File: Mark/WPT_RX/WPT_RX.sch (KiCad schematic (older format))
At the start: 58 parts, among them J1 Conn_01x01, J2 Conn_01x01, J3 SMA, J4 SMA, J5 SMA, J6 Conn_01x01, J7 Conn_01x01, J8 From PI Board, Q1 NMOS, U1 LMC6032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

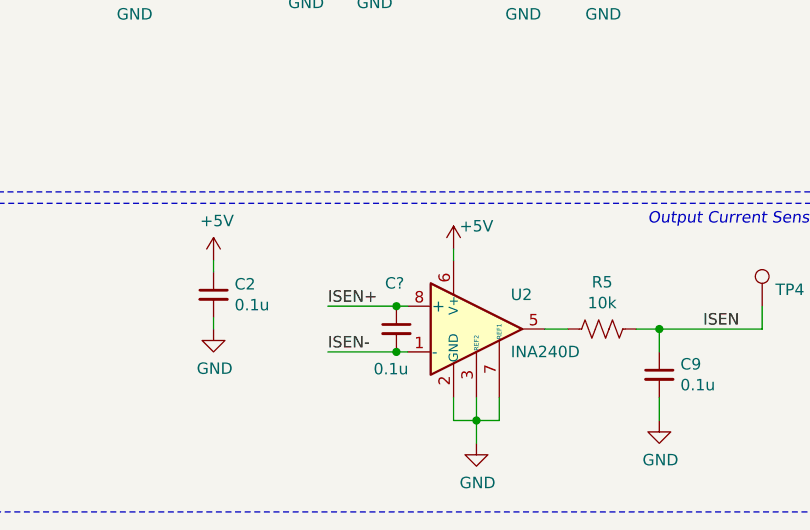
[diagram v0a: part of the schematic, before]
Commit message: More Layout
- Reduced board length, should reduce board cost.
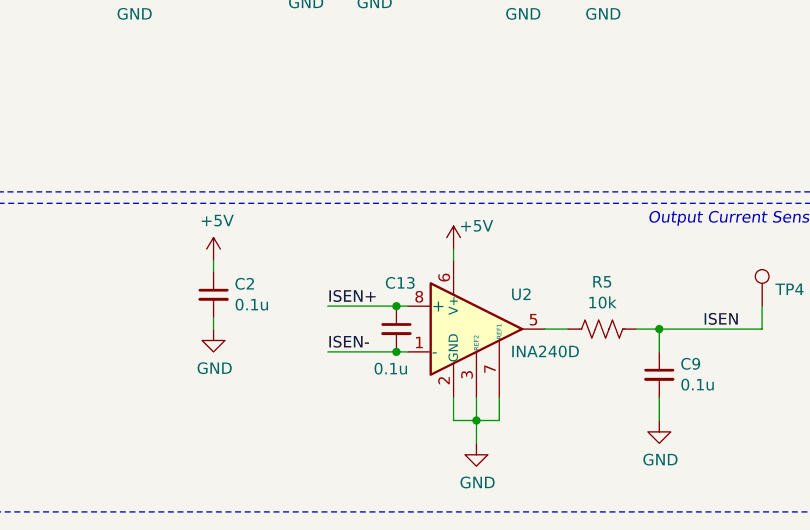
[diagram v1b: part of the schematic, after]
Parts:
- R12, R13, R14, R9: footprint Package_TO_SOT_THT:TO-220F-2_Horizontal_TabDown -> WPT_RX:TO-220F-2_Horizontal_TabDown
- gave numbers to parts that had none: 1
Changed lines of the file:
@@
 F 0 "R9" H 8018 3296 50  0000 L CNN
 F 1 "10R" H 8018 3205 50  0000 L CNN
-F 2 "Package_TO_SOT_THT:TO-220F-2_Horizontal_TabDown" H 8018 3159 50  0001 L CNN
+F 2 "WPT_RX:TO-220F-2_Horizontal_TabDown" H 8018 3159 50  0001 L CNN
 F 3 "~" H 7950 3250 50  0001 C CNN
 F 4 "PWR221T-50-10R0F-ND" H 7950 3250 50  0001 C CNN "Digikey"
@@
 F 0 "R12" H 8318 3296 50  0000 L CNN
 F 1 "10R" H 8318 3205 50  0000 L CNN
-F 2 "Package_TO_SOT_THT:TO-220F-2_Horizontal_TabDown" H 8318 3159 50  0001 L CNN
+F 2 "WPT_RX:TO-220F-2_Horizontal_TabDown" H 8318 3159 50  0001 L CNN
 F 3 "~" H 8250 3250 50  0001 C CNN
 F 4 "PWR221T-50-10R0F-ND" H 8250 3250 50  0001 C CNN "Digikey"
@@
 F 0 "R13" H 8618 3296 50  0000 L CNN
 F 1 "10R" H 8618 3205 50  0000 L CNN
-F 2 "Package_TO_SOT_THT:TO-220F-2_Horizontal_TabDown" H 8618 3159 50  0001 L CNN
+F 2 "WPT_RX:TO-220F-2_Horizontal_TabDown" H 8618 3159 50  0001 L CNN
 F 3 "~" H 8550 3250 50  0001 C CNN
 F 4 "PWR221T-50-10R0F-ND" H 8550 3250 50  0001 C CNN "Digikey"
@@
 F 0 "R14" H 8918 3296 50  0000 L CNN
 F 1 "10R" H 8918 3205 50  0000 L CNN
-F 2 "Package_TO_SOT_THT:TO-220F-2_Horizontal_TabDown" H 8918 3159 50  0001 L CNN
+F 2 "WPT_RX:TO-220F-2_Horizontal_TabDown" H 8918 3159 50  0001 L CNN
 F 3 "~" H 8850 3250 50  0001 C CNN
 F 4 "PWR221T-50-10R0F-ND" H 8850 3250 50  0001 C CNN "Digikey"
@@
 $EndComp
 $Comp
-L Device:C_Small C?
+L Device:C_Small C13
 U 1 1 5FBB5F7F
 P 2500 5250
-F 0 "C?" H 2450 5450 50  0000 L CNN
+F 0 "C13" H 2450 5450 50  0000 L CNN
 F 1 "0.1u" H 2400 5075 50  0000 L CNN
 F 2 "Capacitor_SMD:C_0603_1608Metric" H 2500 5250 50  0001 C CNN

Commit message: Created WPT BOMs
- Created TX and RX BOMs
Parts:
- U1: Digikey (none) -> LMC6032IMX/NOPBCT-ND
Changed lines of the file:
@@
 F 2 "Package_SO:SOIC-8_3.9x4.9mm_P1.27mm" H 4150 3400 50  0001 C CNN
 F 3 "http://www.ti.com/lit/ds/symlink/lmc6082.pdf" H 4150 3400 50  0001 C CNN
-F 4 "" H 4150 3400 50  0001 C CNN "Digikey"
+F 4 "LMC6032IMX/NOPBCT-ND" H 4150 3400 50  0001 C CNN "Digikey"
 	1    4150 3400
 	1    0    0    -1
